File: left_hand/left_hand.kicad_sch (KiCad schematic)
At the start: 39 parts, among them J1 8P8C_Shielded, J2 Conn_01x03, J3 Conn_01x08, J4 Conn_01x08, M1 Motor_Servo, M2 Motor_Servo, M3 Motor_Servo, M4 Motor_Servo, M5 Motor_Servo, Q1 Q_NMOS_GDS, Q2 Q_NMOS_GDS, Q3 Q_NMOS_GDS, Q4 Q_NMOS_GDS, Q5 Q_NMOS_GDS, U1 MCP23017_SP, U2 PCA9615DP, U3 PCA9685PW

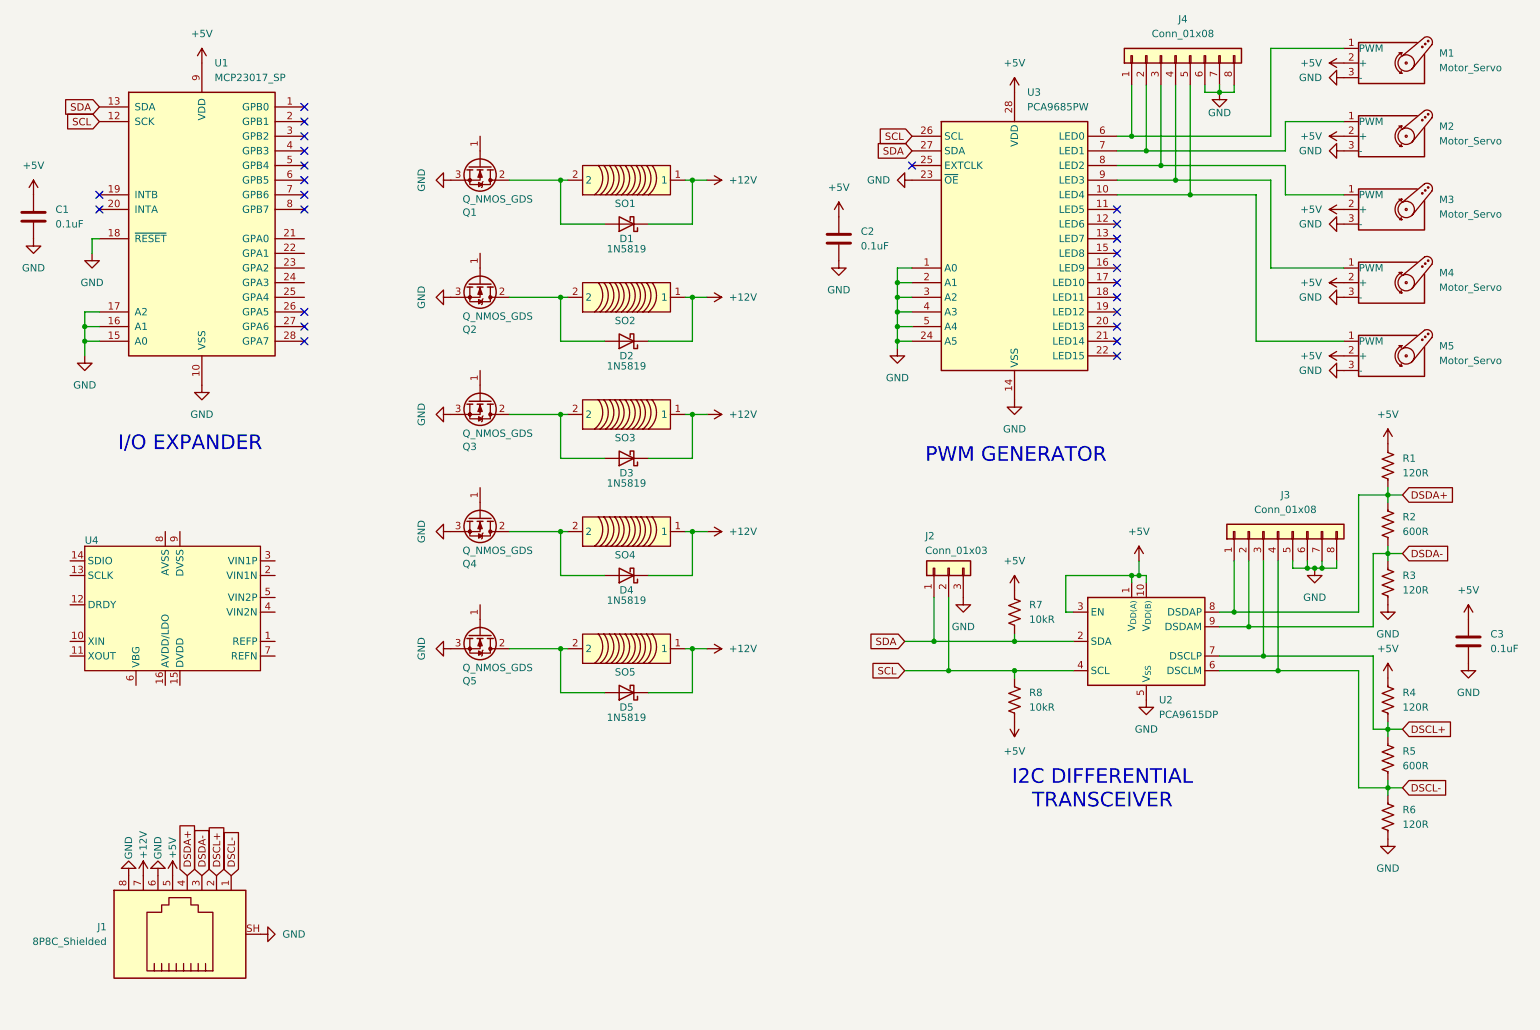
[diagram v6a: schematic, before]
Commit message: Added gate resistors to MOSFETs
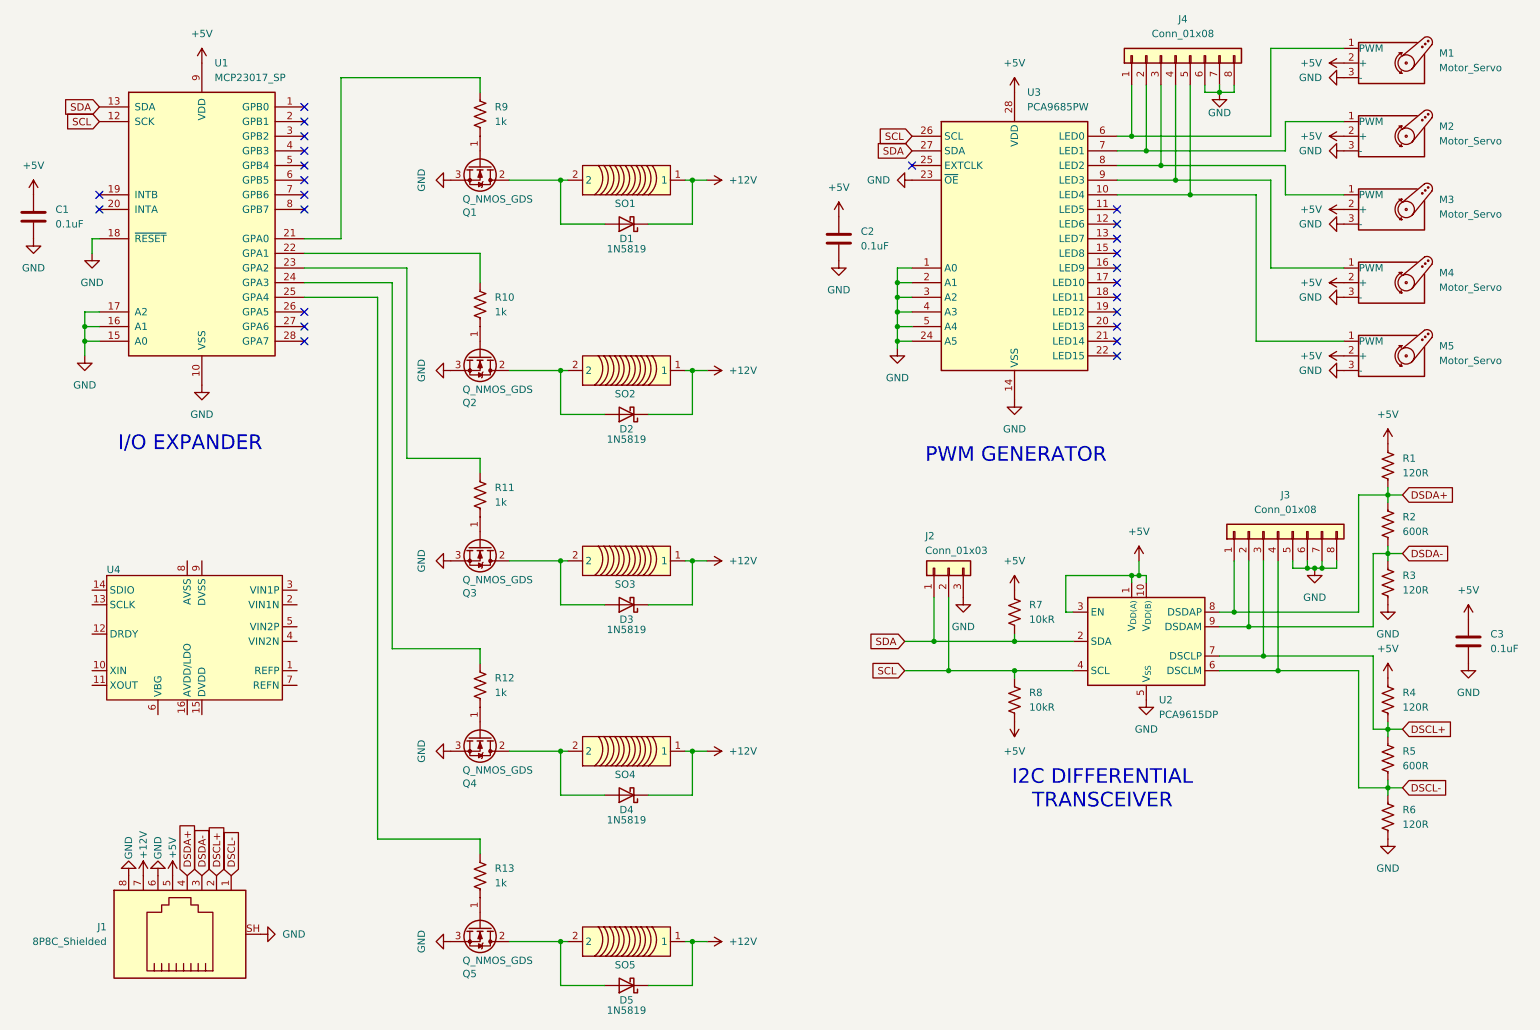
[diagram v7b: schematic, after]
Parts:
- added R10, R11, R12, R13, R9: 1k, symbol Device:R_US
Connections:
- net at Q4.1 (G): now also R12.2
- net at Q3.1 (G): now also R11.2
- net at U1.21 (GPA0): now also R9.1
- net at U1.22 (GPA1): now also R10.1
- net at U1.23 (GPA2): now also R11.1
- net at U1.24 (GPA3): now also R12.1
- net at U1.25 (GPA4): now also R13.1
- net at Q5.1 (G): now also R13.2
- net at Q1.1 (G): now also R9.2
- net at Q2.1 (G): now also R10.2
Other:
- moved on the sheet: U4

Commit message: I2C transceivers, sheet hierarchy changes
Added I2C transceivers for both hands on the controller side, also changed sheet hierarchy to modularize controller board sheet somewhat
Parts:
- M1, M2, M3, M4, M5: footprint (none) -> Connector_PinHeader_2.54mm:PinHeader_1x03_P2.54mm_Horizontal
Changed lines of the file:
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@@
 			)
 		)
-		(property "Footprint" ""
+		(property "Footprint" "Connector_PinHeader_2.54mm:PinHeader_1x03_P2.54mm_Horizontal"
 			(at 256.54 53.086 0)
 			(effects
@@
 			)
 		)
-		(property "Footprint" ""
+		(property "Footprint" "Connector_PinHeader_2.54mm:PinHeader_1x03_P2.54mm_Horizontal"
 			(at 256.54 65.786 0)
 			(effects
@@
 			)
 		)
-		(property "Footprint" ""
+		(property "Footprint" "Connector_PinHeader_2.54mm:PinHeader_1x03_P2.54mm_Horizontal"
 			(at 256.54 78.486 0)
 			(effects
@@
 			)
 		)
-		(property "Footprint" ""
+		(property "Footprint" "Connector_PinHeader_2.54mm:PinHeader_1x03_P2.54mm_Horizontal"
 			(at 256.54 27.686 0)
 			(effects
@@
 			)
 		)
-		(property "Footprint" ""
+		(property "Footprint" "Connector_PinHeader_2.54mm:PinHeader_1x03_P2.54mm_Horizontal"
 			(at 256.54 40.386 0)
 			(effects
